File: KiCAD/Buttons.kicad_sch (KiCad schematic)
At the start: 1 part, among them SW2 SW_Push

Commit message: Start PCB Layout
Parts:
- added SW10_SHARE1, SW11_START1, SW12_THROW1, SW13_R3, SW14_PS1, SW15_TOUCHPAD1, SW16_UP1, SW17_UP2, SW18_DOWN1, SW19_LEFT1, SW20_RIGHT1, SW3_MK1, SW4_LP1, SW5_MP1, SW6_DI1, SW7_HP1, SW8_DP1, SW9_HK1: SW_Push, Fightstick_Library:Kailh_MX_Style_Keyswitch, symbol Switch:SW_Push
- SW2_LK1: renamed from SW2; footprint keyswitches.pretty-2.1:Kailh_socket_MX -> Fightstick_Library:Kailh_MX_Style_Keyswitch
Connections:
- net A1: now also SW14_PS1.1; no longer SW2_LK1.1
- net GND: now also SW10_SHARE1.2, SW11_START1.2, SW12_THROW1.2, SW13_R3.2, SW14_PS1.2, SW15_TOUCHPAD1.2, SW16_UP1.2, SW17_UP2.2, SW18_DOWN1.2, SW19_LEFT1.2, SW20_RIGHT1.2, SW3_MK1.2, SW4_LP1.2, SW5_MP1.2, SW6_DI1.2, SW7_HP1.2, SW8_DP1.2, SW9_HK1.2
- new net A2: SW15_TOUCHPAD1.1
- new net B1: SW2_LK1.1
- new net B2: SW3_MK1.1
- new net B3: SW4_LP1.1
- new net B4: SW5_MP1.1
- new net DOWN: SW18_DOWN1.1
- new net L1: SW6_DI1.1
- new net L2: SW8_DP1.1
- new net L3: SW12_THROW1.1
- new net LEFT: SW19_LEFT1.1
- new net R1: SW7_HP1.1
- new net R2: SW9_HK1.1
- new net R3: SW13_R3.1
- new net RIGHT: SW20_RIGHT1.1
- new net S1: SW10_SHARE1.1
- new net S2: SW11_START1.1
- new net UP1: SW16_UP1.1
- new net UP2: SW17_UP2.1
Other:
- moved on the sheet: SW2_LK1

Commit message: PCB First Draft
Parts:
- removed SW13_R3: SW_Push, Fightstick_Library:Kailh_MX_Style_Keyswitch, symbol Switch:SW_Push
- added SW2_MODE1: SW_SPST, Button_Switch_THT:SW_SPST_Omron_B3F-40xx, symbol Switch:SW_Push
- SW10_SHARE1, SW11_START1, SW14_PS1, SW15_TOUCHPAD1: footprint Fightstick_Library:Kailh_MX_Style_Keyswitch -> Button_Switch_THT:SW_SPST_Omron_B3F-40xx; now left out of the parts list
- SW12_THROW1, SW18_DOWN1, SW19_LEFT1, SW20_RIGHT1, SW2_LK1, SW3_MK1, SW4_LP1, SW5_MP1, SW6_DI1, SW7_HP1, SW8_DP1, SW9_HK1: now left out of the parts list
- SW16_SPACE1: renamed from SW16_UP1; now left out of the parts list
- SW17_W1: renamed from SW17_UP2; now left out of the parts list
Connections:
- net GND: now also SW2_MODE1.2
- net UP1 renamed SPACE
- net UP2 renamed W
- new net MODE: SW2_MODE1.1

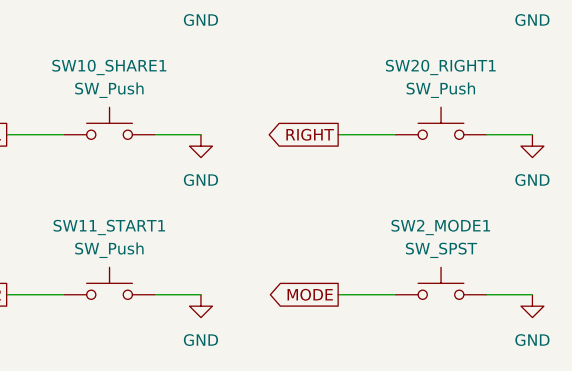
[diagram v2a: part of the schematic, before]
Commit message: Make PCB and case fit together
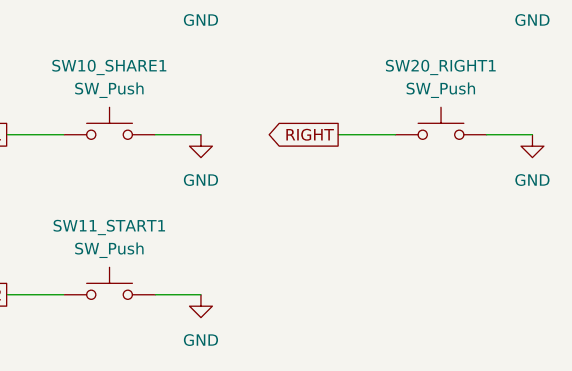
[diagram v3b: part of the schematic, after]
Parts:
- removed SW2_MODE1: SW_SPST, Button_Switch_THT:SW_SPST_Omron_B3F-40xx, symbol Switch:SW_Push
- SW12_THROW1, SW16_SPACE1, SW2_LK1, SW3_MK1, SW4_LP1, SW5_MP1, SW6_DI1, SW7_HP1, SW8_DP1, SW9_HK1: footprint Fightstick_Library:Kailh_MX_Style_Keyswitch -> PCM_Switch_Keyboard_Cherry_MX:SW_Cherry_MX_PCB
- SW17_W1, SW18_DOWN1, SW19_LEFT1, SW20_RIGHT1: footprint Fightstick_Library:Kailh_MX_Style_Keyswitch -> PCM_Switch_Keyboard_Cherry_MX:SW_Cherry_MX_PCB_1.00u

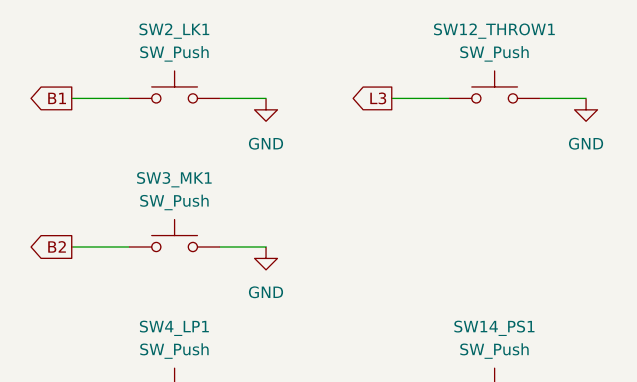
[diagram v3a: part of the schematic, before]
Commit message: Add multiboard configurations
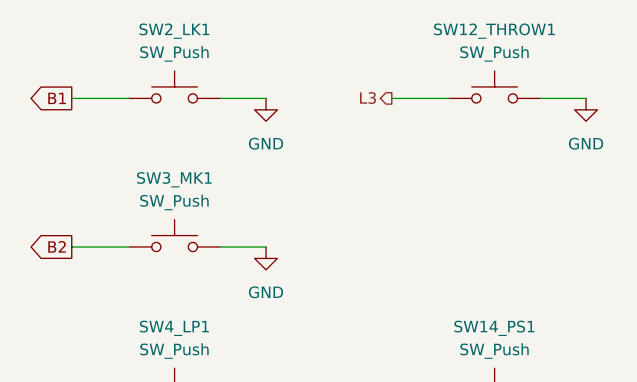
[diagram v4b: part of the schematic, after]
